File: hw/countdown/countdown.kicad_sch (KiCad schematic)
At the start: 24 parts, among them J1 TC2030-SWD, SW1 TS-1187A-B-A-B, U1 STM32L031G6U6, Y1 32.768kHz

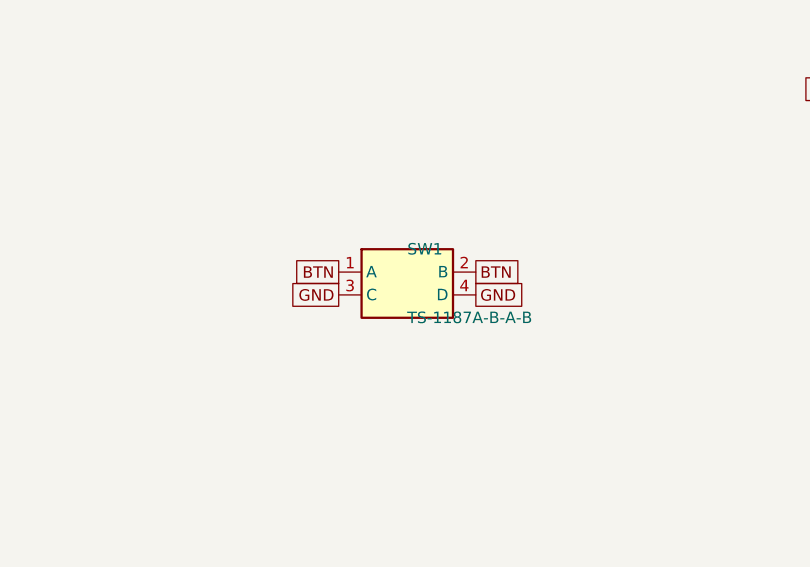
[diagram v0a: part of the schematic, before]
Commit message: Review fixes (fw: BYPSHAD, LSEDRV order, flash staleness, vectors; sch: diagonal switch wiring) + routing endgame tooling
Co-Authored-By: Claude Fable 5 <noreply@anthropic.com>
Claude-Session: https://claude.ai/code/session_01EyK7WVGPpPEnSjWLWWV8on
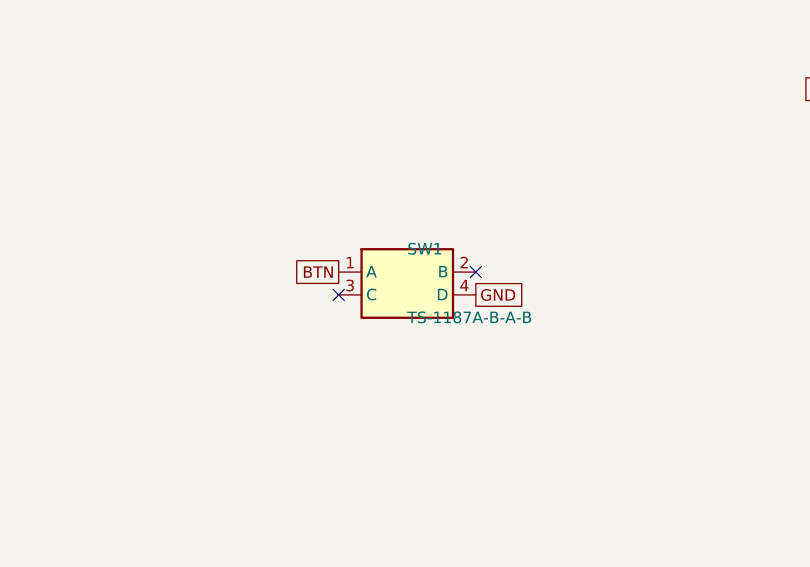
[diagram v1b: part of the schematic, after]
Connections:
- net BTN: no longer SW1.2 (B)
- net GND: no longer SW1.3 (C)
- no-connect marks 5 -> 7
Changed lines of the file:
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@@
 		)
 	)
-	(global_label "GND"
-		(shape passive)
-		(at 152.4 151.13 180)
-		(effects
-			(font
-				(size 1.27 1.27)
-			)
-			(justify right)
-		)
-	)
-	(global_label "BTN"
-		(shape passive)
-		(at 167.64 148.59 0)
-		(effects
-			(font
-				(size 1.27 1.27)
-			)
-			(justify left)
-		)
+	(no_connect
+		(at 152.4 151.13)
+	)
+	(no_connect
+		(at 167.64 148.59)
 	)
 	(global_label "GND"
@@
 		(instances
 			(project "countdown"
-				(path "/e47b4bcb-0c5e-406c-871a-e857463f1509"
+				(path "/2b20cf59-7efc-4a2f-b7c1-0a78851032a1"
 					(reference "U1")
 					(unit 1)
@@
 		(instances
 			(project "countdown"
-				(path "/e47b4bcb-0c5e-406c-871a-e857463f1509"
+				(path "/2b20cf59-7efc-4a2f-b7c1-0a78851032a1"
 					(reference "DS1")
 					(unit 1)
@@
 		(instances
 			(project "countdown"
-				(path "/e47b4bcb-0c5e-406c-871a-e857463f1509"
+				(path "/2b20cf59-7efc-4a2f-b7c1-0a78851032a1"
 					(reference "R1")
 					(unit 1)
@@
 		(instances
 			(project "countdown"
-				(path "/e47b4bcb-0c5e-406c-871a-e857463f1509"
+				(path "/2b20cf59-7efc-4a2f-b7c1-0a78851032a1"
 					(reference "R2")
 					(unit 1)
@@
 		(instances
 			(project "countdown"
-				(path "/e47b4bcb-0c5e-406c-871a-e857463f1509"
+				(path "/2b20cf59-7efc-4a2f-b7c1-0a78851032a1"
 					(reference "R3")
 					(unit 1)
@@
 		(instances
 			(project "countdown"
-				(path "/e47b4bcb-0c5e-406c-871a-e857463f1509"
+				(path "/2b20cf59-7efc-4a2f-b7c1-0a78851032a1"
 					(reference "R4")
 					(unit 1)
@@
 		(instances
 			(project "countdown"
-				(path "/e47b4bcb-0c5e-406c-871a-e857463f1509"
+				(path "/2b20cf59-7efc-4a2f-b7c1-0a78851032a1"
 					(reference "R5")
 					(unit 1)
@@
 		(instances
 			(project "countdown"
-				(path "/e47b4bcb-0c5e-406c-871a-e857463f1509"
+				(path "/2b20cf59-7efc-4a2f-b7c1-0a78851032a1"
 					(reference "R6")
 					(unit 1)
@@
 		(instances
 			(project "countdown"
-				(path "/e47b4bcb-0c5e-406c-871a-e857463f1509"
+				(path "/2b20cf59-7efc-4a2f-b7c1-0a78851032a1"
 					(reference "R7")
 					(unit 1)
@@
 		(instances
 			(project "countdown"
-				(path "/e47b4bcb-0c5e-406c-871a-e857463f1509"
+				(path "/2b20cf59-7efc-4a2f-b7c1-0a78851032a1"
 					(reference "R8")
 					(unit 1)
@@
 		(instances
 			(project "countdown"
-				(path "/e47b4bcb-0c5e-406c-871a-e857463f1509"
+				(path "/2b20cf59-7efc-4a2f-b7c1-0a78851032a1"
 					(reference "R9")
 					(unit 1)
@@
 		(instances
 			(project "countdown"
-				(path "/e47b4bcb-0c5e-406c-871a-e857463f1509"
+				(path "/2b20cf59-7efc-4a2f-b7c1-0a78851032a1"
 					(reference "BT1")
 					(unit 1)
@@
 		(instances
 			(project "countdown"
-				(path "/e47b4bcb-0c5e-406c-871a-e857463f1509"
+				(path "/2b20cf59-7efc-4a2f-b7c1-0a78851032a1"
 					(reference "Y1")
 					(unit 1)
@@
 		(instances
 			(project "countdown"
-				(path "/e47b4bcb-0c5e-406c-871a-e857463f1509"
+				(path "/2b20cf59-7efc-4a2f-b7c1-0a78851032a1"
 					(reference "C7")
 					(unit 1)
@@
 		(instances
 			(project "countdown"
-				(path "/e47b4bcb-0c5e-406c-871a-e857463f1509"
+				(path "/2b20cf59-7efc-4a2f-b7c1-0a78851032a1"
 					(reference "C8")
 					(unit 1)
@@
 		(instances
 			(project "countdown"
-				(path "/e47b4bcb-0c5e-406c-871a-e857463f1509"
+				(path "/2b20cf59-7efc-4a2f-b7c1-0a78851032a1"
 					(reference "C1")
 					(unit 1)
@@
 		(instances
 			(project "countdown"
-				(path "/e47b4bcb-0c5e-406c-871a-e857463f1509"
+				(path "/2b20cf59-7efc-4a2f-b7c1-0a78851032a1"
 					(reference "C2")
 					(unit 1)
@@
 		(instances
 			(project "countdown"
-				(path "/e47b4bcb-0c5e-406c-871a-e857463f1509"
+				(path "/2b20cf59-7efc-4a2f-b7c1-0a78851032a1"
 					(reference "C4")
 					(unit 1)
@@
 		(instances
 			(project "countdown"
-				(path "/e47b4bcb-0c5e-406c-871a-e857463f1509"
+				(path "/2b20cf59-7efc-4a2f-b7c1-0a78851032a1"
 					(reference "C5")
 					(unit 1)
@@
 		(instances
 			(project "countdown"
-				(path "/e47b4bcb-0c5e-406c-871a-e857463f1509"
+				(path "/2b20cf59-7efc-4a2f-b7c1-0a78851032a1"
 					(reference "C6")
 					(unit 1)
@@
 		(instances
 			(project "countdown"
-				(path "/e47b4bcb-0c5e-406c-871a-e857463f1509"
+				(path "/2b20cf59-7efc-4a2f-b7c1-0a78851032a1"
 					(reference "C3")
 					(unit 1)
@@
 		(instances
 			(project "countdown"
-				(path "/e47b4bcb-0c5e-406c-871a-e857463f1509"
+				(path "/2b20cf59-7efc-4a2f-b7c1-0a78851032a1"
 					(reference "SW1")
 					(unit 1)
@@
 		(instances
 			(project "countdown"
-				(path "/e47b4bcb-0c5e-406c-871a-e857463f1509"
+				(path "/2b20cf59-7efc-4a2f-b7c1-0a78851032a1"
 					(reference "J1")
 					(unit 1)
@@
 		(instances
 			(project "countdown"
-				(path "/e47b4bcb-0c5e-406c-871a-e857463f1509"
+				(path "/2b20cf59-7efc-4a2f-b7c1-0a78851032a1"
 					(reference "H1")
 					(unit 1)
@@
 		(instances
 			(project "countdown"
-				(path "/e47b4bcb-0c5e-406c-871a-e857463f1509"
+				(path "/2b20cf59-7efc-4a2f-b7c1-0a78851032a1"
 					(reference "#FLG01")
 					(unit 1)
@@
 		(instances
 			(project "countdown"
-				(path "/e47b4bcb-0c5e-406c-871a-e857463f1509"
+				(path "/2b20cf59-7efc-4a2f-b7c1-0a78851032a1"
 					(reference "#FLG02")
 					(unit 1)

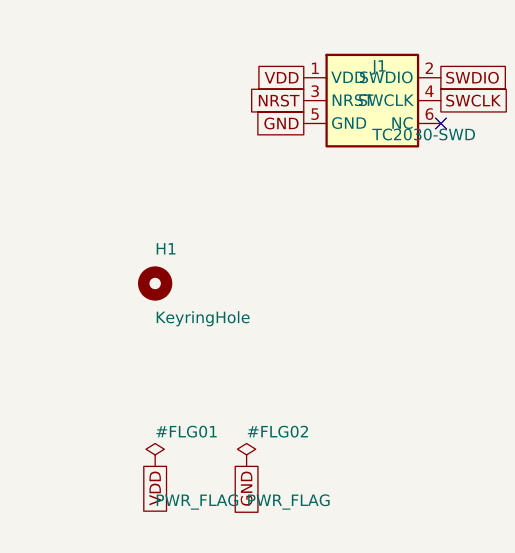
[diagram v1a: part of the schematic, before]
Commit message: Footprint/DFM review fixes: GND-only vias under QFN, via spacing gates, plated GND keyring ring, display pads to true terminal width, silk cleanup + hidden refs
Co-Authored-By: Claude Fable 5 <noreply@anthropic.com>
Claude-Session: https://claude.ai/code/session_01EyK7WVGPpPEnSjWLWWV8on
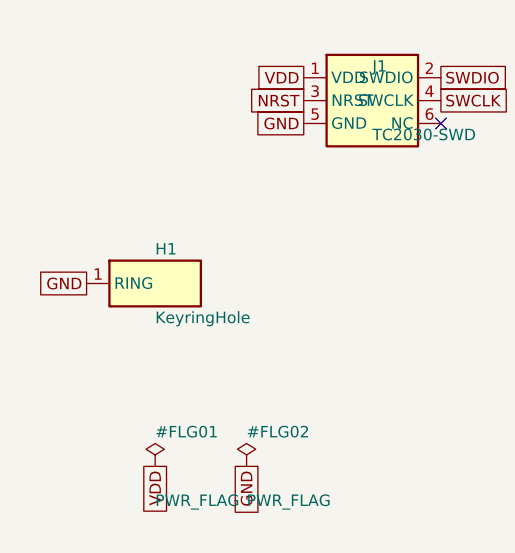
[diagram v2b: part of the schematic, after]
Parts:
- removed H1: KeyringHole, countdown:KeyringHole_4mm, symbol Mechanical:MountingHole
- added H1: KeyringHole, countdown:KeyringHole_4mm, symbol countdown:KEYRING_HOLE
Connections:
- net GND: now also H1.1 (RING)
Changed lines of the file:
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@@
 		(at 52.07 152.4)
+	)
+	(global_label "GND"
+		(shape passive)
+		(at 12.7 170.18 180)
+		(effects
+			(font
+				(size 1.27 1.27)
+			)
+			(justify right)
+		)
 	)
 	(global_label "VDD"
@@
 		(instances
 			(project "countdown"
-				(path "/2b20cf59-7efc-4a2f-b7c1-0a78851032a1"
+				(path "/11ae53a9-2e61-48ea-ac28-a73746a3e841"
 					(reference "U1")
 					(unit 1)
@@
 		(instances
 			(project "countdown"
-				(path "/2b20cf59-7efc-4a2f-b7c1-0a78851032a1"
+				(path "/11ae53a9-2e61-48ea-ac28-a73746a3e841"
 					(reference "DS1")
 					(unit 1)
@@
 		(instances
 			(project "countdown"
-				(path "/2b20cf59-7efc-4a2f-b7c1-0a78851032a1"
+				(path "/11ae53a9-2e61-48ea-ac28-a73746a3e841"
 					(reference "R1")
 					(unit 1)
@@
 		(instances
 			(project "countdown"
-				(path "/2b20cf59-7efc-4a2f-b7c1-0a78851032a1"
+				(path "/11ae53a9-2e61-48ea-ac28-a73746a3e841"
 					(reference "R2")
 					(unit 1)
@@
 		(instances
 			(project "countdown"
-				(path "/2b20cf59-7efc-4a2f-b7c1-0a78851032a1"
+				(path "/11ae53a9-2e61-48ea-ac28-a73746a3e841"
 					(reference "R3")
 					(unit 1)
@@
 		(instances
 			(project "countdown"
-				(path "/2b20cf59-7efc-4a2f-b7c1-0a78851032a1"
+				(path "/11ae53a9-2e61-48ea-ac28-a73746a3e841"
 					(reference "R4")
 					(unit 1)
@@
 		(instances
 			(project "countdown"
-				(path "/2b20cf59-7efc-4a2f-b7c1-0a78851032a1"
+				(path "/11ae53a9-2e61-48ea-ac28-a73746a3e841"
 					(reference "R5")
 					(unit 1)
@@
 		(instances
 			(project "countdown"
-				(path "/2b20cf59-7efc-4a2f-b7c1-0a78851032a1"
+				(path "/11ae53a9-2e61-48ea-ac28-a73746a3e841"
 					(reference "R6")
 					(unit 1)
@@
 		(instances
 			(project "countdown"
-				(path "/2b20cf59-7efc-4a2f-b7c1-0a78851032a1"
+				(path "/11ae53a9-2e61-48ea-ac28-a73746a3e841"
 					(reference "R7")
 					(unit 1)
@@
 		(instances
 			(project "countdown"
-				(path "/2b20cf59-7efc-4a2f-b7c1-0a78851032a1"
+				(path "/11ae53a9-2e61-48ea-ac28-a73746a3e841"
 					(reference "R8")
 					(unit 1)
@@
 		(instances
 			(project "countdown"
-				(path "/2b20cf59-7efc-4a2f-b7c1-0a78851032a1"
+				(path "/11ae53a9-2e61-48ea-ac28-a73746a3e841"
 					(reference "R9")
 					(unit 1)
@@
 		(instances
 			(project "countdown"
-				(path "/2b20cf59-7efc-4a2f-b7c1-0a78851032a1"
+				(path "/11ae53a9-2e61-48ea-ac28-a73746a3e841"
 					(reference "BT1")
 					(unit 1)
@@
 		(instances
 			(project "countdown"
-				(path "/2b20cf59-7efc-4a2f-b7c1-0a78851032a1"
+				(path "/11ae53a9-2e61-48ea-ac28-a73746a3e841"
 					(reference "Y1")
 					(unit 1)
@@
 		(instances
 			(project "countdown"
-				(path "/2b20cf59-7efc-4a2f-b7c1-0a78851032a1"
+				(path "/11ae53a9-2e61-48ea-ac28-a73746a3e841"
 					(reference "C7")
 					(unit 1)
@@
 		(instances
 			(project "countdown"
-				(path "/2b20cf59-7efc-4a2f-b7c1-0a78851032a1"
+				(path "/11ae53a9-2e61-48ea-ac28-a73746a3e841"
 					(reference "C8")
 					(unit 1)
@@
 		(instances
 			(project "countdown"
-				(path "/2b20cf59-7efc-4a2f-b7c1-0a78851032a1"
+				(path "/11ae53a9-2e61-48ea-ac28-a73746a3e841"
 					(reference "C1")
 					(unit 1)
@@
 		(instances
 			(project "countdown"
-				(path "/2b20cf59-7efc-4a2f-b7c1-0a78851032a1"
+				(path "/11ae53a9-2e61-48ea-ac28-a73746a3e841"
 					(reference "C2")
 					(unit 1)
@@
 		(instances
 			(project "countdown"
-				(path "/2b20cf59-7efc-4a2f-b7c1-0a78851032a1"
+				(path "/11ae53a9-2e61-48ea-ac28-a73746a3e841"
 					(reference "C4")
 					(unit 1)
@@
 		(instances
 			(project "countdown"
-				(path "/2b20cf59-7efc-4a2f-b7c1-0a78851032a1"
+				(path "/11ae53a9-2e61-48ea-ac28-a73746a3e841"
 					(reference "C5")
 					(unit 1)
@@
 		(instances
 			(project "countdown"
-				(path "/2b20cf59-7efc-4a2f-b7c1-0a78851032a1"
+				(path "/11ae53a9-2e61-48ea-ac28-a73746a3e841"
 					(reference "C6")
 					(unit 1)
@@
 		(instances
 			(project "countdown"
-				(path "/2b20cf59-7efc-4a2f-b7c1-0a78851032a1"
+				(path "/11ae53a9-2e61-48ea-ac28-a73746a3e841"
 					(reference "C3")
 					(unit 1)
@@
 		(instances
 			(project "countdown"
-				(path "/2b20cf59-7efc-4a2f-b7c1-0a78851032a1"
+				(path "/11ae53a9-2e61-48ea-ac28-a73746a3e841"
 					(reference "SW1")
 					(unit 1)
@@
 		(instances
 			(project "countdown"
-				(path "/2b20cf59-7efc-4a2f-b7c1-0a78851032a1"
+				(path "/11ae53a9-2e61-48ea-ac28-a73746a3e841"
 					(reference "J1")
 					(unit 1)
@@
 	)
 	(symbol
-		(lib_id "Mechanical:MountingHole")
+		(lib_id "countdown:KEYRING_HOLE")
 		(at 20.32 170.18 0)
 		(unit 1)
@@
 			)
 		)
-		(instances
-			(project "countdown"
-				(path "/2b20cf59-7efc-4a2f-b7c1-0a78851032a1"
+		(pin "1"
+		)
+		(instances
+			(project "countdown"
+				(path "/11ae53a9-2e61-48ea-ac28-a73746a3e841"
 					(reference "H1")
 					(unit 1)
@@
 		(instances
 			(project "countdown"
-				(path "/2b20cf59-7efc-4a2f-b7c1-0a78851032a1"
+				(path "/11ae53a9-2e61-48ea-ac28-a73746a3e841"
 					(reference "#FLG01")
 					(unit 1)
@@
 		(instances
 			(project "countdown"
-				(path "/2b20cf59-7efc-4a2f-b7c1-0a78851032a1"
+				(path "/11ae53a9-2e61-48ea-ac28-a73746a3e841"
 					(reference "#FLG02")
 					(unit 1)
